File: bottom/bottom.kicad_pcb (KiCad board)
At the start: 2 copper layers, 499.9 x 141.3 mm, 14 parts

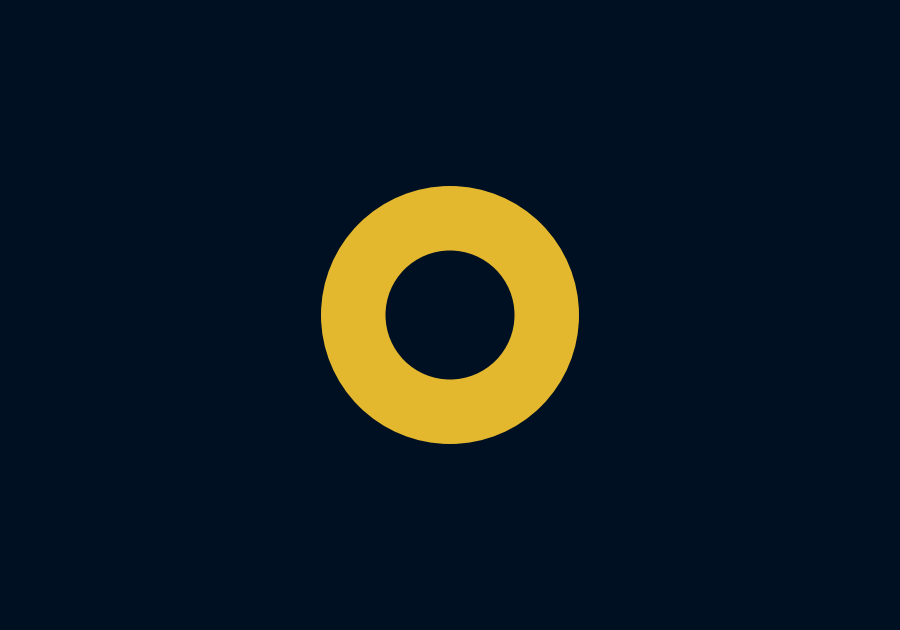
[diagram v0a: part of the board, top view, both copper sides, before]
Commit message: fix D1 and space stab holes
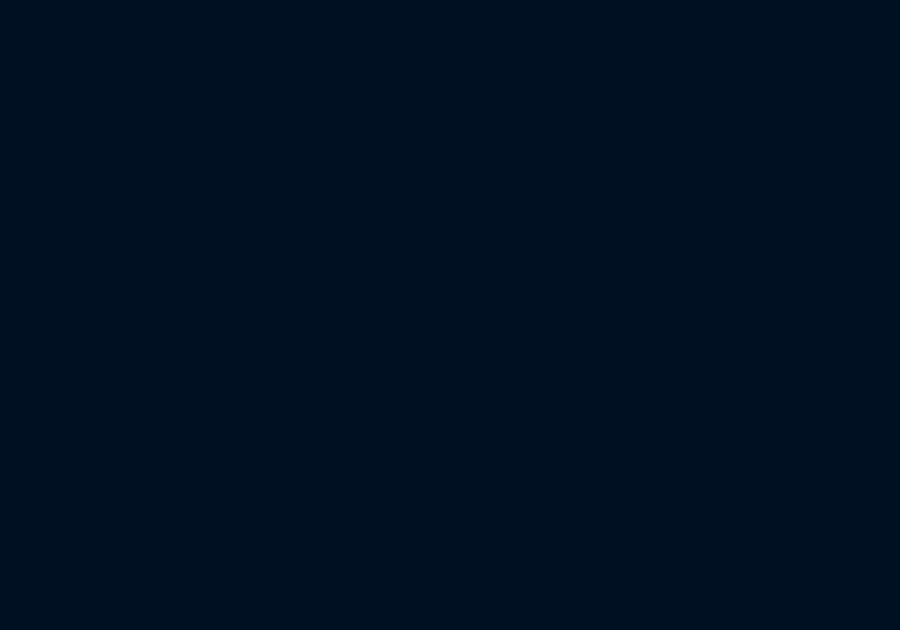
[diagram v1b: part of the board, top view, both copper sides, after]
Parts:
- removed H13: MountingHole_4.3mm_M4_Pad, MountingHole:MountingHole_4.3mm_M4_Pad
- added G***: LOGO, xt:star, F.Cu at (312.3, 280.8)
- added G***: LOGO, xt:letters, B.Cu at (248.3, 290.6)
- added G***: LOGO, xt:crack, B.Cu at (240.3, 291.4)
